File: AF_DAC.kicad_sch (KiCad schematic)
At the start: 28 parts, among them J9 3.5mm_Jack, U10 PAM8908, U9 CJC4334H

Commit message: Lots of signal traces wided
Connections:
- net at C62.1, R50.2: now also U10.3 (INR+); no longer U10.2 (INL+)
- net at TP8.1, U10.5 (OUTR): now also J9.R; no longer J9.T
- net at TP7.1, U10.16 (OUTL): now also J9.T; no longer J9.R
- net at C61.1, R49.2: now also U10.2 (INL+); no longer U10.3 (INR+)
- net at C69.2, R53.1, e4.2 (B): no longer J9.S
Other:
- moved on the sheet: J9
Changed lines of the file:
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@@
-	(wire
-		(pts
-			(xy 224.79 96.52) (xy 224.79 91.44)
-		)
-		(stroke
-			(width 0)
-			(type default)
-		)
-	)
 	(wire
 		(pts
@@
 	(wire
 		(pts
-			(xy 151.13 93.98) (xy 135.89 93.98)
-		)
-		(stroke
-			(width 0)
-			(type default)
-		)
-	)
-	(wire
-		(pts
 			(xy 217.17 86.36) (xy 224.79 86.36)
 		)
@@
 	(wire
 		(pts
+			(xy 151.13 97.79) (xy 151.13 93.98)
+		)
+		(stroke
+			(width 0)
+			(type default)
+		)
+	)
+	(wire
+		(pts
 			(xy 226.06 105.41) (xy 226.06 106.68)
 		)
@@
 	(wire
 		(pts
-			(xy 132.08 83.82) (xy 132.08 97.79)
-		)
-		(stroke
-			(width 0)
-			(type default)
-		)
-	)
-	(wire
-		(pts
 			(xy 72.39 60.96) (xy 83.82 60.96)
 		)
@@
 	(wire
 		(pts
-			(xy 135.89 93.98) (xy 135.89 80.01)
-		)
-		(stroke
-			(width 0)
-			(type default)
-		)
-	)
-	(wire
-		(pts
-			(xy 115.57 97.79) (xy 132.08 97.79)
+			(xy 115.57 97.79) (xy 151.13 97.79)
 		)
 		(stroke
@@
 	(wire
 		(pts
-			(xy 135.89 80.01) (xy 115.57 80.01)
+			(xy 115.57 80.01) (xy 151.13 80.01)
 		)
 		(stroke
@@
 	(wire
 		(pts
-			(xy 151.13 83.82) (xy 132.08 83.82)
-		)
-		(stroke
-			(width 0)
-			(type default)
-		)
-	)
-	(wire
-		(pts
 			(xy 181.61 104.14) (xy 185.42 104.14)
 		)
@@
 	(wire
 		(pts
+			(xy 224.79 91.44) (xy 224.79 96.52)
+		)
+		(stroke
+			(width 0)
+			(type default)
+		)
+	)
+	(wire
+		(pts
 			(xy 151.13 76.2) (xy 151.13 78.74)
 		)
@@
 		(pts
 			(xy 95.25 80.01) (xy 100.33 80.01)
+		)
+		(stroke
+			(width 0)
+			(type default)
+		)
+	)
+	(wire
+		(pts
+			(xy 151.13 80.01) (xy 151.13 83.82)
 		)
 		(stroke
@@
 	(symbol
 		(lib_id "Connector_Audio:AudioJack2_Ground")
-		(at 229.87 91.44 0)
-		(mirror y)
+		(at 229.87 88.9 180)
 		(unit 1)
 		(body_style 1)
@@
 		(dnp no)
 		(property "Reference" "J9"
-			(at 234.95 92.075 0)
+			(at 234.95 88.265 0)
 			(show_name no)
 			(do_not_autoplace no)
@@
 		)
 		(property "Value" "3.5mm_Jack"
-			(at 224.79 83.82 0)
+			(at 224.79 96.52 0)
 			(hide yes)
 			(show_name no)
@@
 		)
 		(property "Footprint" "Intro_to_CAD:Jack_3.5mm_CUI_SJ-3523-SMT_Horizontal"
-			(at 229.87 91.44 0)
+			(at 229.87 88.9 0)
 			(hide yes)
 			(show_name no)
@@
 		)
 		(property "Datasheet" "https://www.lcsc.com/datasheet/lcsc_datasheet_1811132022_BOOMELE-Boom-Precision-Elec-PJ-320B_C18594.pdf"
-			(at 229.87 91.44 0)
+			(at 229.87 88.9 0)
 			(hide yes)
 			(show_name no)
@@
 		)
 		(property "Description" "DAC OUT"
-			(at 230.632 85.344 0)
+			(at 230.632 94.996 0)
 			(show_name no)
 			(do_not_autoplace no)
@@
 		)
 		(property "LCSC" "C18594"
-			(at 229.87 91.44 0)
+			(at 229.87 88.9 0)
 			(hide yes)
 			(show_name no)
@@
 		)
 		(property "JLCPCB #" ""
-			(at 229.87 91.44 0)
-			(hide yes)
-			(show_name no)
+			(at 229.87 88.9 0)
+			(hide yes)
+			(show_name no)

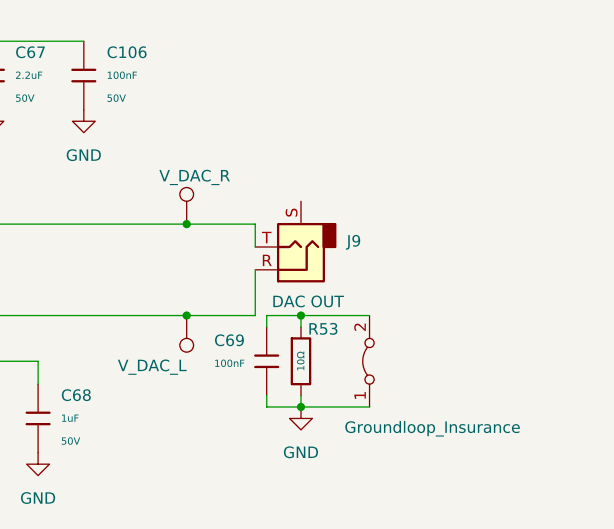
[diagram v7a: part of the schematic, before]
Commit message: PAM and LEDs
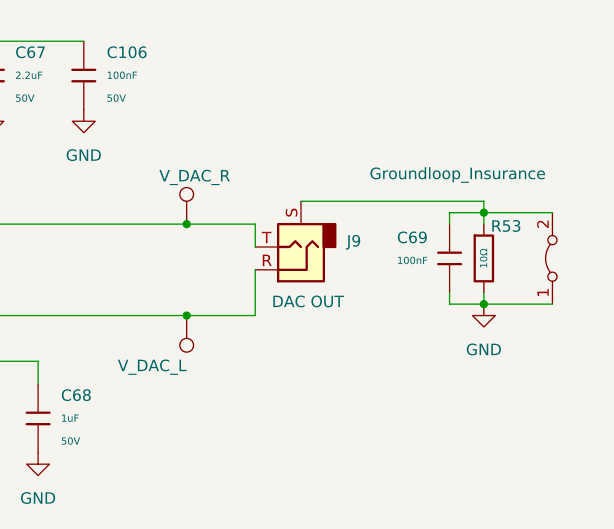
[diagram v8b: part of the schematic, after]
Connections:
- net at J9.S: now also C69.2, R53.1, e4.2 (B)
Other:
- moved on the sheet: C69, R53
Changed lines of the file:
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@@
 	)
 	(junction
-		(at 229.87 96.52)
+		(at 250.19 85.09)
 		(diameter 0)
 		(color 0 0 0 0)
@@
 	)
 	(junction
-		(at 229.87 106.68)
+		(at 250.19 95.25)
 		(diameter 0)
 		(color 0 0 0 0)
@@
 	(wire
 		(pts
-			(xy 226.06 96.52) (xy 229.87 96.52)
+			(xy 246.38 85.09) (xy 250.19 85.09)
 		)
 		(stroke
@@
 	(wire
 		(pts
-			(xy 229.87 97.79) (xy 229.87 96.52)
+			(xy 250.19 86.36) (xy 250.19 85.09)
 		)
 		(stroke
@@
 	(wire
 		(pts
-			(xy 237.49 96.52) (xy 229.87 96.52)
+			(xy 257.81 85.09) (xy 250.19 85.09)
 		)
 		(stroke
@@
 	(wire
 		(pts
-			(xy 226.06 105.41) (xy 226.06 106.68)
+			(xy 246.38 93.98) (xy 246.38 95.25)
 		)
 		(stroke
@@
 	(wire
 		(pts
+			(xy 229.87 83.82) (xy 250.19 83.82)
+		)
+		(stroke
+			(width 0)
+			(type default)
+		)
+	)
+	(wire
+		(pts
 			(xy 166.37 109.22) (xy 168.91 109.22)
 		)
@@
 	(wire
 		(pts
+			(xy 250.19 83.82) (xy 250.19 85.09)
+		)
+		(stroke
+			(width 0)
+			(type default)
+		)
+	)
+	(wire
+		(pts
 			(xy 142.24 110.49) (xy 142.24 106.68)
 		)
@@
 	(wire
 		(pts
-			(xy 226.06 106.68) (xy 229.87 106.68)
+			(xy 246.38 95.25) (xy 250.19 95.25)
 		)
 		(stroke
@@
 	(wire
 		(pts
-			(xy 226.06 97.79) (xy 226.06 96.52)
+			(xy 246.38 86.36) (xy 246.38 85.09)
 		)
 		(stroke
@@
 	(wire
 		(pts
-			(xy 229.87 106.68) (xy 237.49 106.68)
+			(xy 250.19 95.25) (xy 257.81 95.25)
 		)
 		(stroke
@@
 	(wire
 		(pts
-			(xy 229.87 105.41) (xy 229.87 106.68)
+			(xy 250.19 93.98) (xy 250.19 95.25)
 		)
 		(stroke
@@
 		(lib_name "GND_1")
 		(lib_id "power:GND")
-		(at 229.87 106.68 0)
+		(at 250.19 95.25 0)
 		(unit 1)
 		(body_style 1)
@@
 		(fields_autoplaced yes)
 		(property "Reference" "#PWR0101"
-			(at 229.87 113.03 0)
+			(at 250.19 101.6 0)
 			(hide yes)
 			(show_name no)
@@
 		)
 		(property "Value" "GND"
-			(at 229.87 111.76 0)
+			(at 250.19 100.33 0)
 			(show_name no)
 			(do_not_autoplace no)
@@
 		)
 		(property "Footprint" ""
-			(at 229.87 106.68 0)
+			(at 250.19 95.25 0)
 			(hide yes)
 			(show_name no)
@@
 		)
 		(property "Datasheet" ""
-			(at 229.87 106.68 0)
+			(at 250.19 95.25 0)
 			(hide yes)
 			(show_name no)
@@
 		)
 		(property "Description" ""
-			(at 229.87 106.68 0)
+			(at 250.19 95.25 0)
 			(hide yes)
 			(show_name no)
@@
 	(symbol
 		(lib_id "PCM_JLCPCB-Resistors:0603,10Ω")
-		(at 229.87 101.6 0)
+		(at 250.19 90.17 0)
 		(unit 1)
 		(body_style 1)
@@
 		(dnp no)
 		(property "Reference" "R53"
-			(at 230.632 98.044 0)
+			(at 250.952 86.614 0)
 			(show_name no)
 			(do_not_autoplace no)
@@
 		)
 		(property "Value" "10Ω"
-			(at 229.87 101.6 90)
+			(at 250.19 90.17 90)
 			(show_name no)
 			(do_not_autoplace yes)
@@
 		)
 		(property "Footprint" "PCM_JLCPCB:R_0603"
-			(at 228.092 101.6 90)
+			(at 248.412 90.17 90)
 			(hide yes)
 			(show_name no)
@@
 		)
 		(property "Datasheet" "https://www.lcsc.com/datasheet/lcsc_datasheet_2206010130_UNI-ROYAL-Uniroyal-Elec-0603WAF100JT5E_C22859.pdf"
-			(at 229.87 101.6 0)
+			(at 250.19 90.17 0)
 			(hide yes)
 			(show_name no)
@@
 		)
 		(property "Description" "100mW Thick Film Resistors 75V ±1% ±400ppm/°C 10Ω 0603 Chip Resistor - Surface Mount ROHS"
-			(at 229.87 101.6 0)
+			(at 250.19 90.17 0)
 			(hide yes)
 			(show_name no)
@@
 		)
 		(property "LCSC" "C22859"
-			(at 229.87 101.6 0)
+			(at 250.19 90.17 0)
 			(hide yes)
 			(show_name no)
@@
 		)
 		(property "Stock" "5764851"
-			(at 229.87 101.6 0)
+			(at 250.19 90.17 0)
 			(hide yes)
 			(show_name no)
@@
 		)
 		(property "Price" "0.004USD"
-			(at 229.87 101.6 0)
+			(at 250.19 90.17 0)
 			(hide yes)
 			(show_name no)
@@
 		)
 		(property "Process" "SMT"
-			(at 229.87 101.6 0)
+			(at 250.19 90.17 0)
 			(hide yes)
 			(show_name no)
@@
 		)
 		(property "Minimum Qty" "20"
-			(at 229.87 101.6 0)
+			(at 250.19 90.17 0)
 			(hide yes)
 			(show_name no)
@@
 		)
 		(property "Attrition Qty" "10"
-			(at 229.87 101.6 0)
+			(at 250.19 90.17 0)
 			(hide yes)
 			(show_name no)
@@
 		)
 		(property "Class" "Basic Component"
-			(at 229.87 101.6 0)
+			(at 250.19 90.17 0)
 			(hide yes)
 			(show_name no)
@@
 		)
 		(property "Category" "Resistors,Chip Resistor - Surface Mount"
-			(at 229.87 101.6 0)
+			(at 250.19 90.17 0)
 			(hide yes)
 			(show_name no)
@@
 		)
 		(property "Part" "0603WAF100JT5E"
-			(at 229.87 101.6 0)
+			(at 250.19 90.17 0)
 			(hide yes)
 			(show_name no)
@@
 		)
 		(property "Resistance" "10Ω"
-			(at 229.87 101.6 0)
+			(at 250.19 90.17 0)
 			(hide yes)
 			(show_name no)
@@
 		)
 		(property "Power(Watts)" "100mW"
-			(at 229.87 101.6 0)
+			(at 250.19 90.17 0)
 			(hide yes)
 			(show_name no)
@@
 		)
 		(property "Type" "Thick Film Resistors"
-			(at 229.87 101.6 0)
+			(at 250.19 90.17 0)
 			(hide yes)
 			(show_name no)
@@
 		)
 		(property "Overload Voltage (Max)" "75V"
-			(at 229.87 101.6 0)
+			(at 250.19 90.17 0)
 			(hide yes)
 			(show_name no)
@@
 		)
 		(property "Operating Temperature Range" "-55°C~+155°C"
-			(at 229.87 101.6 0)
+			(at 250.19 90.17 0)
 			(hide yes)
 			(show_name no)
@@
 		)
 		(property "Tolerance" "±1%"
-			(at 229.87 101.6 0)
+			(at 250.19 90.17 0)
 			(hide yes)
 			(show_name no)
@@
 		)
 		(property "Temperature Coefficient" "±400ppm/°C"
-			(at 229.87 101.6 0)
+			(at 250.19 90.17 0)
 			(hide yes)
 			(show_name no)
@@
 	(symbol
 		(lib_id "PCM_JLCPCB-Capacitors:0402,100nF,(2)")
-		(at 226.06 101.6 180)
+		(at 246.38 90.17 180)
 		(unit 1)
 		(body_style 1)
@@
 		(dnp no)
 		(property "Reference" "C69"
-			(at 220.218 99.3139 0)
+			(at 240.538 87.8839 0)
 			(show_name no)
 			(do_not_autoplace no)
@@
 		)
 		(property "Value" "100nF"
-			(at 220.218 101.854 0)
+			(at 240.538 90.424 0)
 			(show_name no)
 			(do_not_autoplace no)
@@
 		)
 		(property "Footprint" "PCM_JLCPCB:C_0402"
-			(at 227.838 101.6 90)
+			(at 248.158 90.17 90)
 			(hide yes)
 			(show_name no)
@@
 		)
 		(property "Datasheet" "https://www.lcsc.com/datasheet/lcsc_datasheet_2304140030_Samsung-Electro-Mechanics-CL05B104KB54PNC_C307331.pdf"
-			(at 226.06 101.6 0)
+			(at 246.38 90.17 0)
 			(hide yes)
 			(show_name no)
@@
 		)
 		(property "Description" "50V 100nF X7R ±10% 0402 Multilayer Ceramic Capacitors MLCC - SMD/SMT ROHS"
-			(at 226.06 101.6 0)
+			(at 246.38 90.17 0)
 			(hide yes)
 			(show_name no)
@@
 		)
 		(property "LCSC" "C307331"
-			(at 226.06 101.6 0)
+			(at 246.38 90.17 0)
 			(hide yes)
 			(show_name no)
@@
 		)
 		(property "Stock" "8389599"
-			(at 226.06 101.6 0)
+			(at 246.38 90.17 0)
 			(hide yes)
 			(show_name no)
@@
 		)
 		(property "Price" "0.008USD"
-			(at 226.06 101.6 0)
+			(at 246.38 90.17 0)
 			(hide yes)
 			(show_name no)
@@
 		)
 		(property "Process" "SMT"
-			(at 226.06 101.6 0)
+			(at 246.38 90.17 0)
 			(hide yes)
 			(show_name no)
@@
 		)
 		(property "Minimum Qty" "20"
-			(at 226.06 101.6 0)
+			(at 246.38 90.17 0)
 			(hide yes)
 			(show_name no)
@@
 		)
 		(property "Attrition Qty" "10"
-			(at 226.06 101.6 0)
+			(at 246.38 90.17 0)
 			(hide yes)
 			(show_name no)
@@
 		)
 		(property "Class" "Basic Component"
-			(at 226.06 101.6 0)
+			(at 246.38 90.17 0)
 			(hide yes)
 			(show_name no)
@@
 		)
 		(property "Category" "Capacitors,Multilayer Ceramic Capacitors MLCC - SMD/SMT"
-			(at 226.06 101.6 0)
+			(at 246.38 90.17 0)
 			(hide yes)
 			(show_name no)
@@
 		)
 		(property "Part" "CL05B104KB54PNC"
-			(at 226.06 101.6 0)
+			(at 246.38 90.17 0)
 			(hide yes)
 			(show_name no)
@@
 		)
 		(property "Voltage Rated" "50V"
-			(at 224.028 99.5538 0)
+			(at 244.348 88.1238 0)
 			(hide yes)
 			(show_name no)
@@
 		)
 		(property "Tolerance" "±10%"
-			(at 226.06 101.6 0)
+			(at 246.38 90.17 0)
 			(hide yes)
 			(show_name no)
@@
 		)
 		(property "Capacitance" "100nF"
-			(at 226.06 101.6 0)
+			(at 246.38 90.17 0)
 			(hide yes)
 			(show_name no)
@@
 		)
 		(property "Temperature Coefficient" "X7R"
-			(at 226.06 101.6 0)
+			(at 246.38 90.17 0)
 			(hide yes)
 			(show_name no)
@@
 		)
 		(property "Manufacturer" "Samsung Electro-Mechanics"
-			(at 226.06 101.6 0)
+			(at 246.38 90.17 0)
 			(hide yes)
 			(show_name no)
@@
 		(lib_name "Jumper_2_Bridged_1")
 		(lib_id "Jumper:Jumper_2_Bridged")
-		(at 237.49 101.6 90)
+		(at 257.81 90.17 90)
 		(unit 1)
 		(body_style 1)
@@
 		(dnp no)
 		(property "Reference" "e4"
-			(at 238.76 100.3299 90)
+			(at 259.08 88.8999 90)
 			(hide yes)
 			(show_name no)
@@
 		)
 		(property "Value" "Groundloop_Insurance"
-			(at 234.696 108.966 90)
+			(at 237.49 80.772 90)
 			(show_name no)
 			(do_not_autoplace no)
@@
 		)
 		(property "Footprint" "Jumper:SolderJumper-2_P1.3mm_Bridged_RoundedPad1.0x1.5mm"
-			(at 237.49 101.6 0)
+			(at 257.81 90.17 0)
 			(hide yes)
 			(show_name no)
@@
 		)
 		(property "Datasheet" ""
-			(at 237.49 101.6 0)
+			(at 257.81 90.17 0)
 			(hide yes)
 			(show_name no)
@@
 		)
 		(property "Description" "Jumper, 2-pole, closed/bridged"
-			(at 237.49 101.6 0)
+			(at 257.81 90.17 0)
 			(hide yes)
 			(show_name no)
